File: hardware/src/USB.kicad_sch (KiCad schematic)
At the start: 24 parts, among them J301 USB_C_Receptacle_USB2.0_16P, Q301 NPN, Q302 NPN, U301 CP2102N-Axx-xQFN24

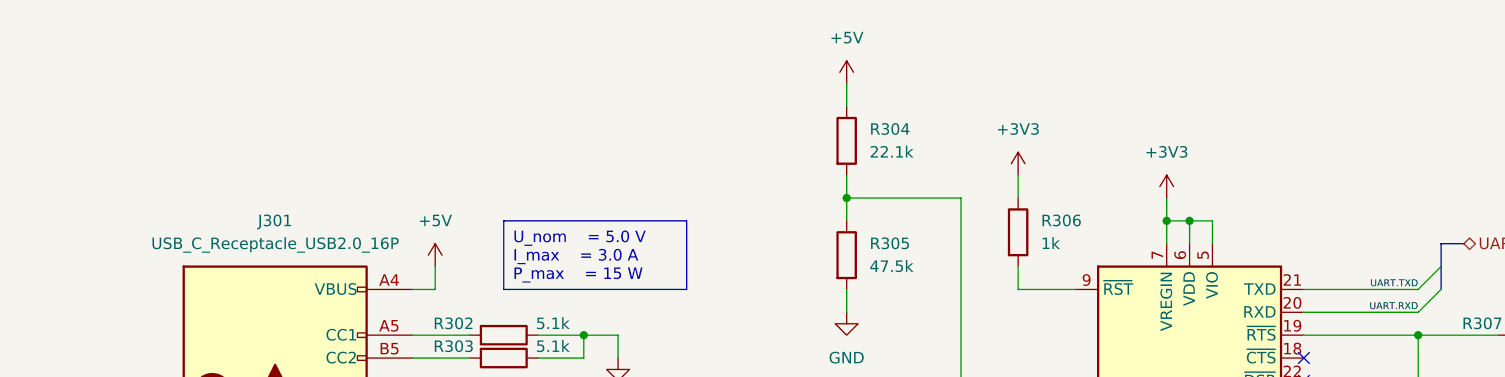
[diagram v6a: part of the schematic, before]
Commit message: Add: Text Headers to the indidual schematic regions
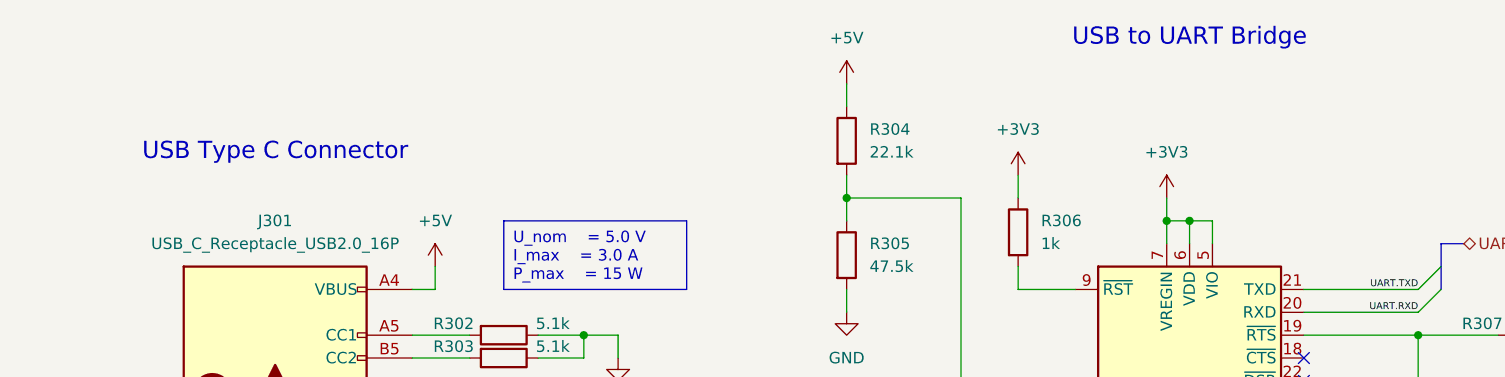
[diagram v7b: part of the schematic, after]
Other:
- note added: "USB Type C Connector"
- note added: "USB to UART Bridge"
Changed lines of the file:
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@@
+		)
+	)
+	(text "USB Type C Connector"
+		(exclude_from_sim no)
+		(at 50.8 50.8 0)
+		(effects
+			(font
+				(size 1.905 1.905)
+			)
 		)
 	)
@@
 		)
 	)
+	(text "USB to UART Bridge"
+		(exclude_from_sim no)
+		(at 152.4 38.1 0)
+		(effects
+			(font
+				(size 1.905 1.905)
+			)
+		)
+	)

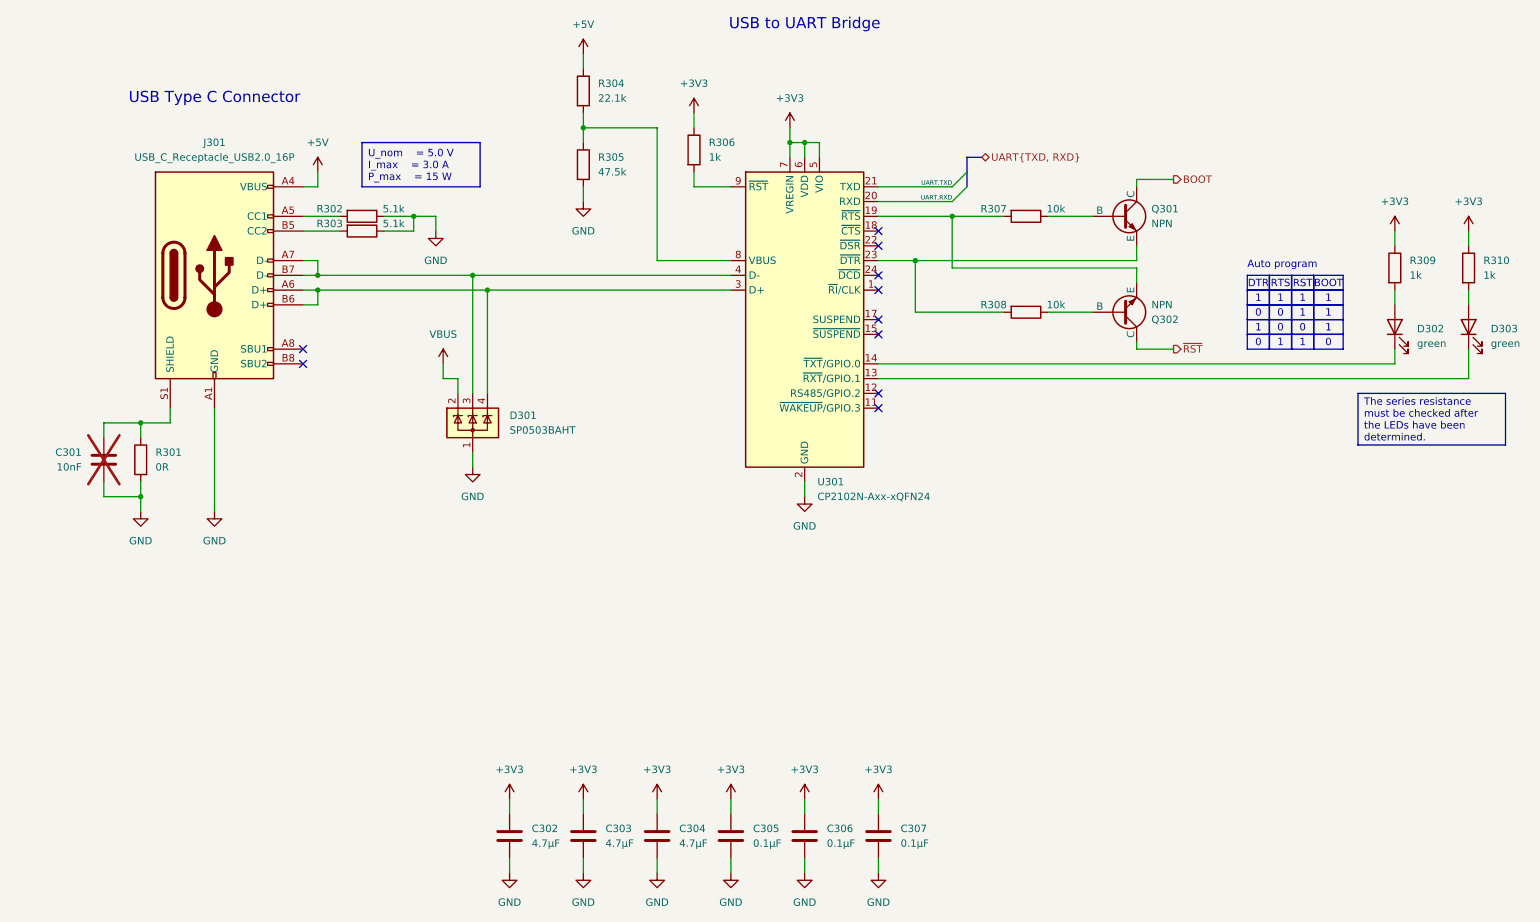
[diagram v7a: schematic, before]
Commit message: Mod: UART, changed position where the TXD and RXD are switched
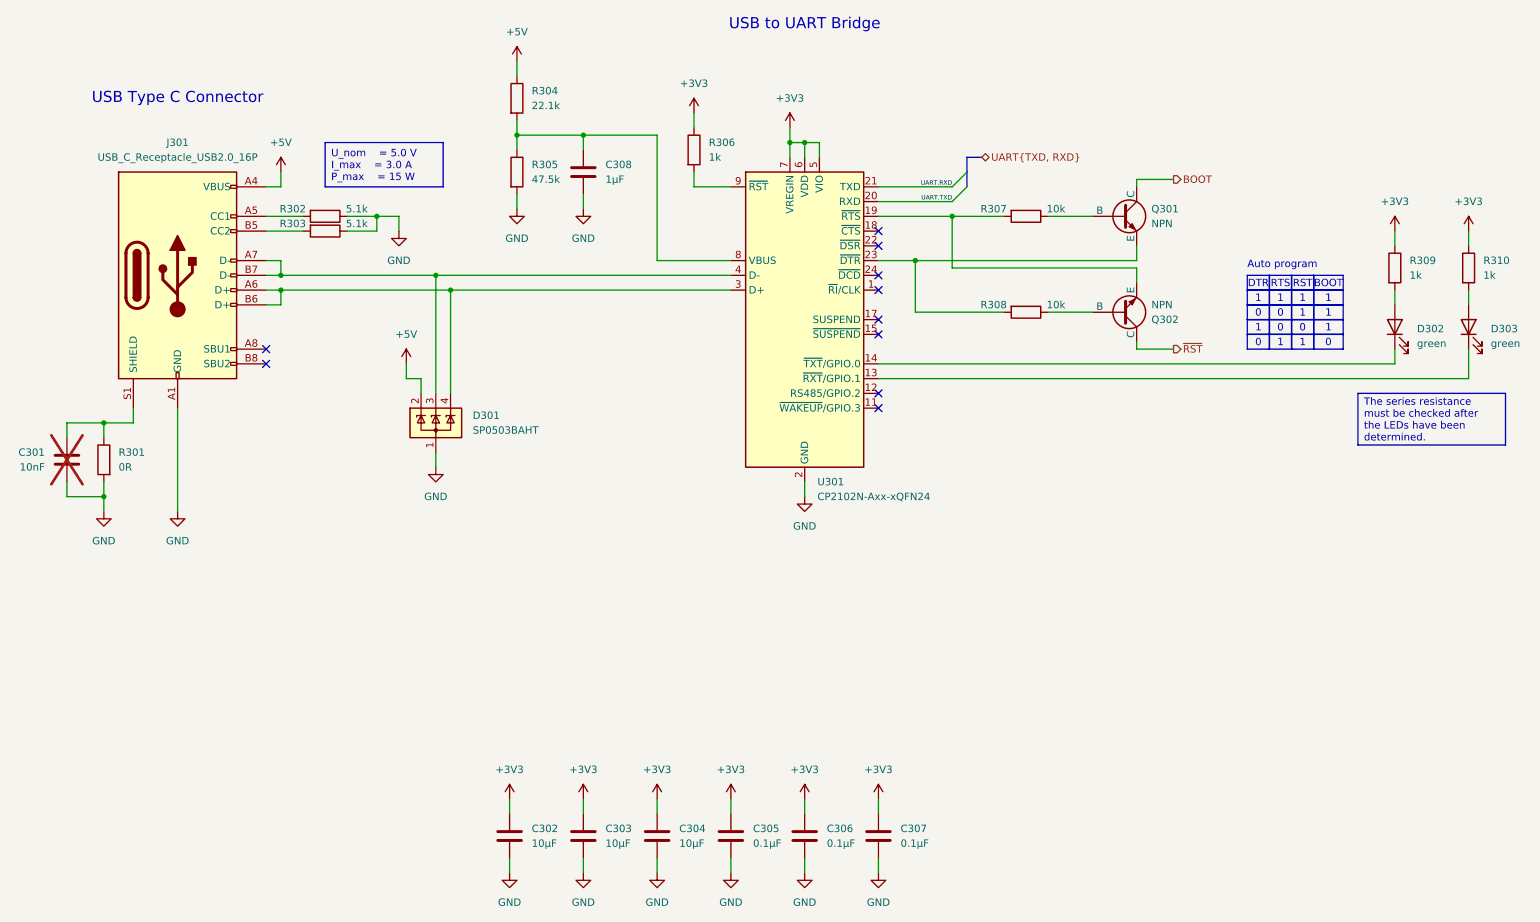
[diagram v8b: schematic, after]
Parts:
- added C308: 1µF, symbol Device:C
- C302, C303, C304: value 4.7µF -> 10µF
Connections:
- net VBUS is gone; now on net +5V: D301.2 (K)
- net GND: now also C308.2
- net UART.RXD: now also U301.21 (TXD); no longer U301.20 (RXD)
- net UART.TXD: now also U301.20 (RXD); no longer U301.21 (TXD)
- net at R304.2, R305.1, U301.8 (VBUS): now also C308.1
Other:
- moved on the sheet: C301, D301, J301, R301, R302, R303, R304, R305
